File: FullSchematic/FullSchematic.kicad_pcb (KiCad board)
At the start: 2 copper layers, 106 parts, among them J1 USB_A, J10 LCD_Conn, J2 ATX-24, J3 Red Banana Jack, J4 Black Banana Jack, J5 2x6 Pin Header, J6 2x6 Pin Header, J7 CT3151-2, J8 CT3151-2, J9 2x6 Pin Header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

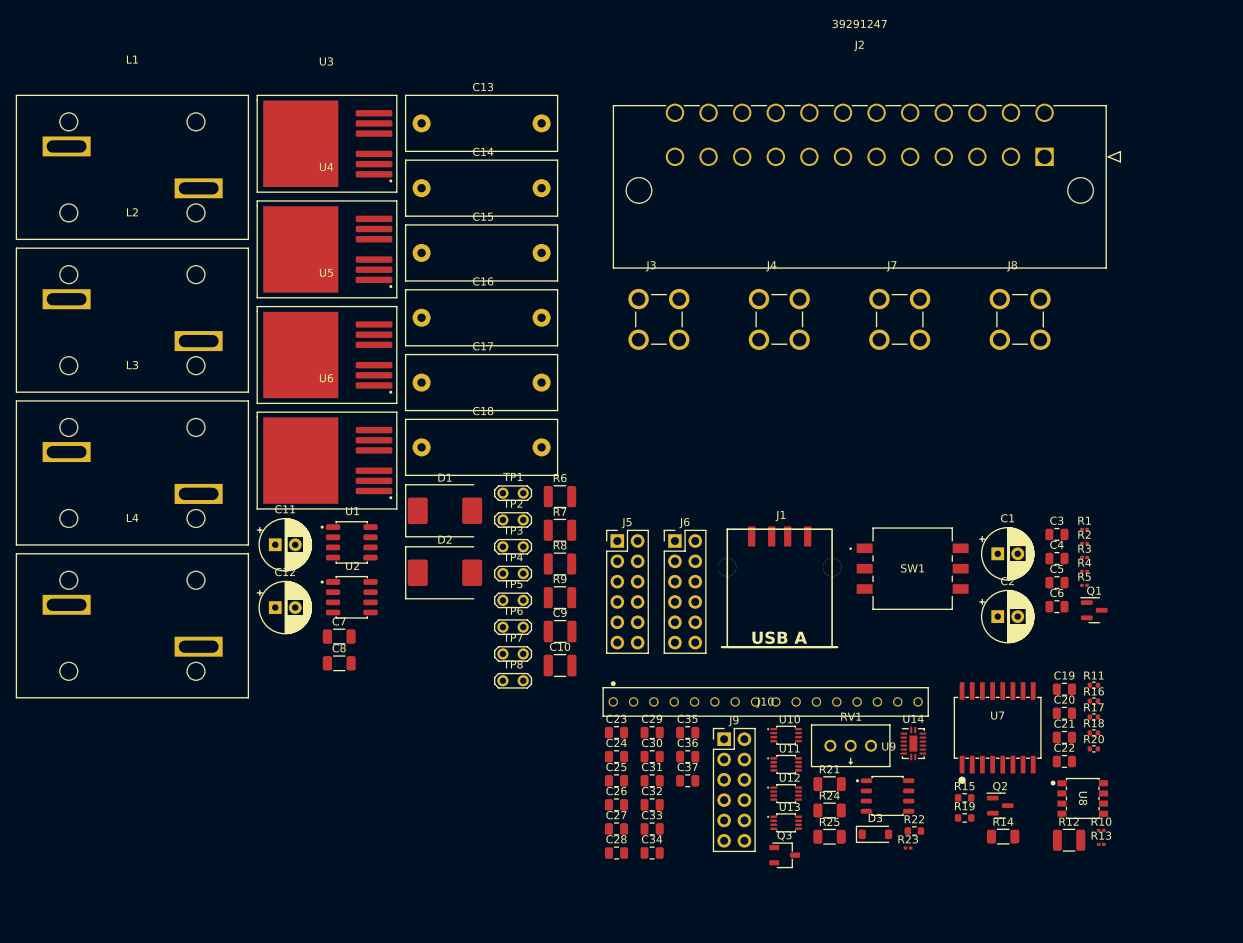
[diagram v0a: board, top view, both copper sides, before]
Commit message: Made PCB a 4-layer board
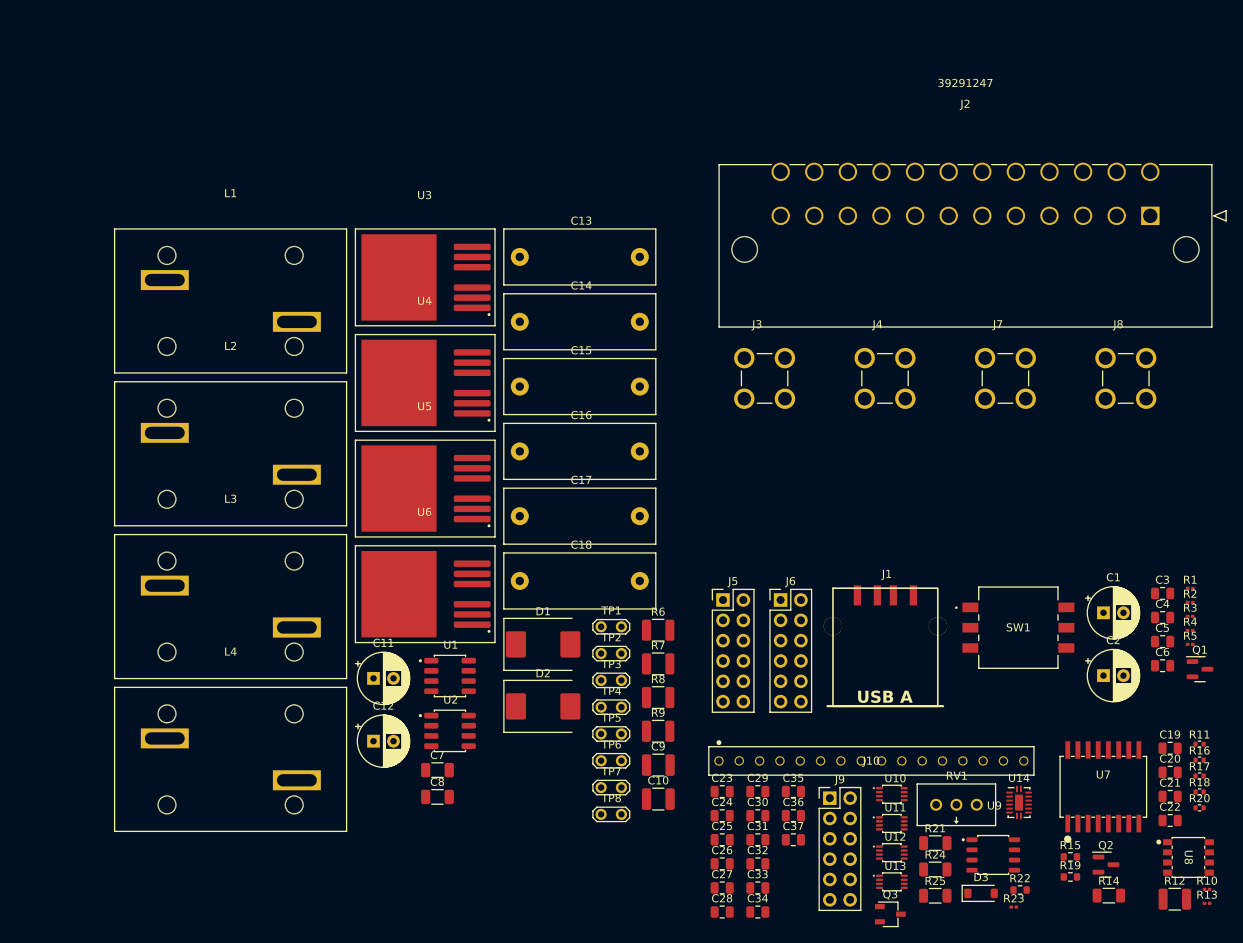
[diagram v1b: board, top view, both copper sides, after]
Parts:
- moved C13 20.7 mm to (145.1, 68.6)
- moved C14 20.7 mm to (145.1, 76.7)
- moved C16 20.7 mm to (145.1, 92.9)
- moved C17 20.7 mm to (145.1, 101.0)
- moved C18 20.7 mm to (145.1, 109.1)
- moved L1 20.7 mm to (101.4, 74.1)
- moved L2 20.7 mm to (101.4, 93.2)
- moved L4 20.7 mm to (101.4, 131.4)
- moved U3 20.7 mm to (122.5, 71.2)
- moved U4 20.7 mm to (122.5, 84.4)
- moved U6 20.7 mm to (122.5, 110.8)
- moved TP6 20.7 mm to (147.7, 131.6)
- moved C11 20.7 mm to (119.3, 121.3)
- moved C12 20.7 mm to (119.3, 129.2)
- moved C15 20.7 mm to (145.1, 84.8)
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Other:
- copper layers 2 -> 4

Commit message: Some Re-arrangements for Power Amplifier
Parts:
- moved C13 223.3 mm to (-74.0, 25.5)
- moved C14 223.3 mm to (-74.0, 33.6)
- moved C15 223.3 mm to (-74.0, 41.7)
- moved C16 223.3 mm to (-74.0, 49.8)
- moved C17 223.3 mm to (-74.0, 57.9)
- moved C18 223.3 mm to (-74.0, 66.0)
- moved C11 177.8 mm to (-58.0, 108.0)
- moved C12 177.8 mm to (-58.0, 115.9)
- moved C7 177.8 mm to (-50.0, 119.5)
- moved C8 177.8 mm to (-50.0, 122.8)
- moved TP1 177.8 mm to (-29.6, 101.6)
- moved TP2 177.8 mm to (-29.6, 104.9)
- moved TP3 177.8 mm to (-29.6, 108.3)
- moved TP4 177.8 mm to (-29.6, 111.6)
- moved TP5 177.8 mm to (-29.6, 115.0)
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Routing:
- net Net-(U1-HO): track 0.00 -> 12.0 mm

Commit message: First attempt at FET/Driver layout
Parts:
- moved C18 353.9 mm to (248.9, -78.8), turned to 90 degrees
- moved C16 337.8 mm to (238.4, -78.8), turned to 90 degrees
- moved C15 331.2 mm to (247.0, -39.5), turned to 90 degrees
- moved C17 330.5 mm to (226.9, -78.8), turned to 90 degrees
- moved C14 319.5 mm to (237.0, -39.5), turned to 90 degrees
- moved C13 305.4 mm to (219.1, -60.3), turned to 90 degrees
- moved TP1 274.0 mm to (152.5, -103.2)
- moved TP2 272.2 mm to (152.4, -97.5)
- moved TP3 269.3 mm to (152.3, -90.3)
- moved C11 268.9 mm to (124.2, -89.8)
- moved J1 265.7 mm to (7.29, -74.2)
- moved TP5 259.8 mm to (152.5, -70.4)
- moved TP7 259.8 mm to (152.5, -63.7)
- moved TP8 259.8 mm to (152.5, -60.4)
- moved C12 259.8 mm to (124.0, -69.5)
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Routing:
- net Net-(U2-VS): track 0.00 -> 122.0 mm, vias 0 -> 2
- net Net-(U1-VS): track 0.00 -> 118.0 mm, vias 0 -> 2
- net COM: track 0.00 -> 81.2 mm, vias 0 -> 6
- net Net-(U5-Gate): track 0.00 -> 37.0 mm
- net Net-(U3-Gate): track 0.00 -> 36.5 mm
- net Net-(U4-Gate): track 0.00 -> 34.2 mm
- net Net-(D1-K): track 0.00 -> 20.7 mm
- net Net-(U1-LO): track 0.00 -> 20.1 mm, vias 0 -> 2
- net +12V: track 0.00 -> 14.1 mm, vias 0 -> 2
- net Net-(U1-HO): track 12.0 -> 4.61 mm
- net Net-(D2-K): track 0.00 -> 4.62 mm
- net Net-(U2-HO): track 0.00 -> 4.36 mm
- added copper zone on In2.Cu, net +12V
- added copper zone on In1.Cu, net COM

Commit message: More Edits
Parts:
- moved J2 259.3 mm to (122.6, 46.2), turned to 180 degrees
- moved R9 85.6 mm to (183.8, 159.8)
- moved U6 85.6 mm to (199.4, 156.2)
- moved U2 85.6 mm to (175.5, 154.4)
- moved U5 85.6 mm to (199.4, 141.1)
- moved C10 85.6 mm to (175.2, 143.2)
- moved C8 85.6 mm to (175.4, 160.7)
- moved D2 85.6 mm to (165.7, 143.2)
- moved R8 85.6 mm to (183.7, 153.7)
- moved U4 33.6 mm to (161.4, 90.7), turned to -90 degrees
- moved U3 30.9 mm to (161.4, 66.8), turned to -90 degrees
- moved D1 30.1 mm to (124.9, 72.1)
- moved U1 30.1 mm to (134.2, 82.5)
- moved C7 30.1 mm to (134.4, 88.4)
- moved C9 30.1 mm to (134.4, 72.1)
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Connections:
- R6 pad 2: Net-(U3-Gate) -> Net-(U1-VS)
- U3 pad 1: Net-(U3-Gate) -> Net-(U1-VS)
- U3 pad TAB: +12V -> Net-(U1-VS)
- U4 pad 5: COM -> Net-(U1-VS)
- U4 pad 6: COM -> Net-(U1-VS)
- U4 pad 7: COM -> Net-(U1-VS)
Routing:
- net COM: track 81.2 -> 143.0 mm
- net Net-(U1-VS): track 118.0 -> 59.7 mm, vias 2 -> 3
- net Net-(U3-Gate): track 36.5 -> 0.00 mm
- net Net-(U4-Gate): track 34.2 -> 0.05 mm
- net Net-(U1-LO): track 20.1 -> 0.00 mm, vias 2 -> 0
- net Net-(D1-K): track 20.7 -> 4.62 mm
- net +12V: track 14.1 -> 3.50 mm, vias 2 -> 1
- net Net-(U1-HO): track 4.61 -> 0.00 mm

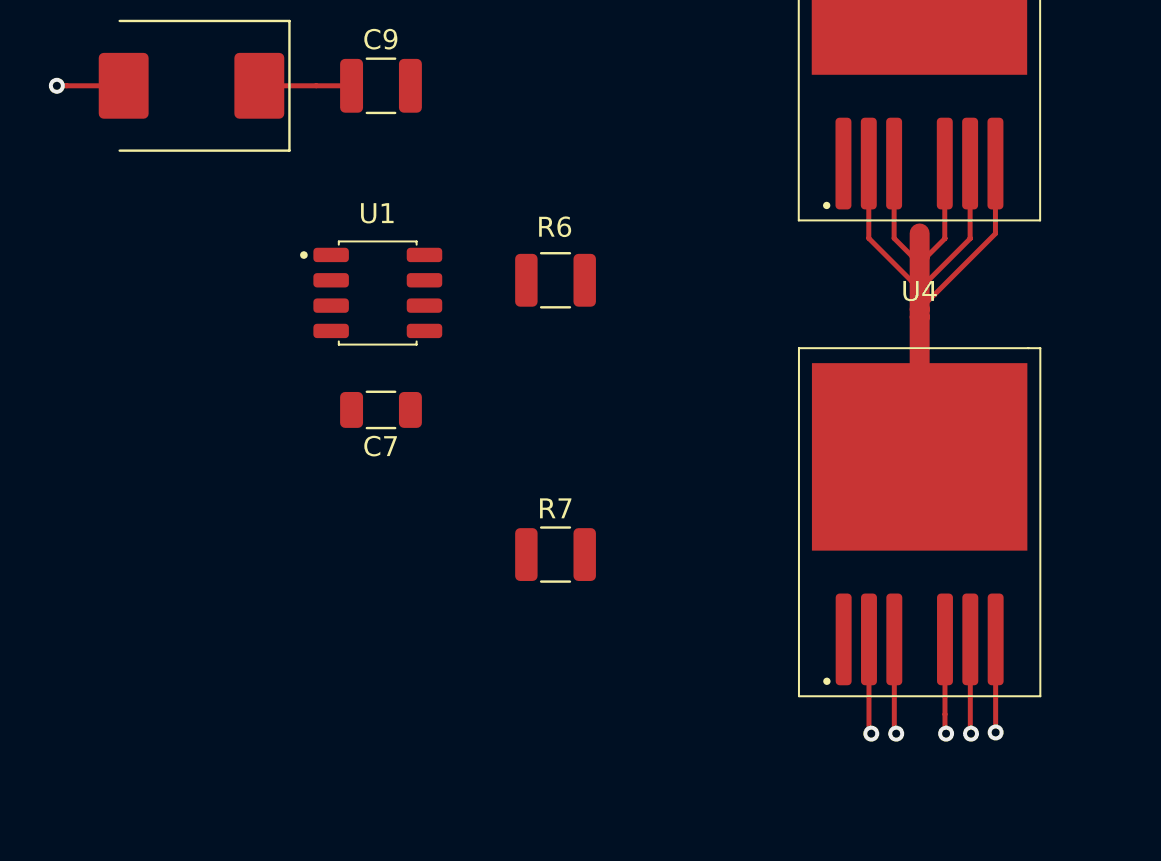
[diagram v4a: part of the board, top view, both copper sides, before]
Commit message: Added high-current power planes on all 4 layers for FETs
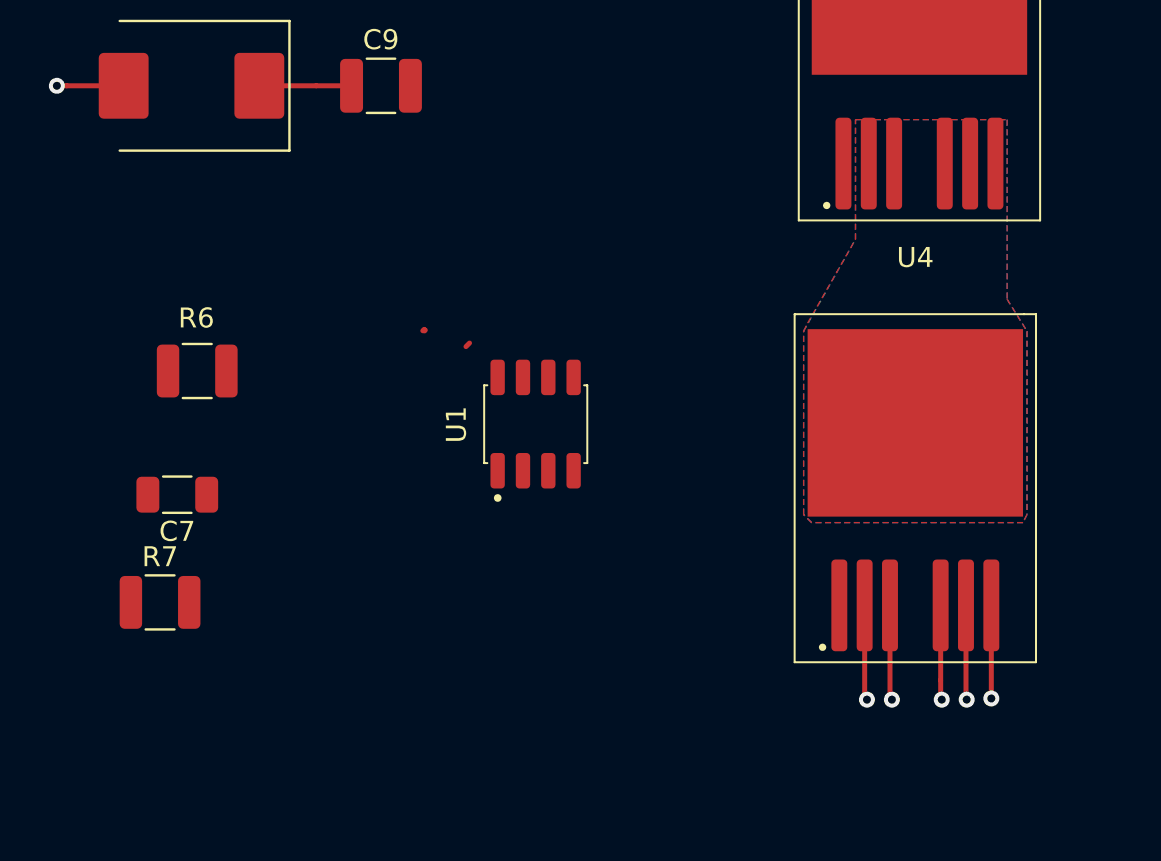
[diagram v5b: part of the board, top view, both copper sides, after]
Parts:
- moved R7 20.0 mm to (123.3, 98.0)
- moved R6 18.5 mm to (125.2, 86.4)
- moved C7 11.1 mm to (124.2, 92.6)
- moved U1 10.3 mm to (142.2, 89.1), turned to 90 degrees
- moved U4 1.72 mm to (161.2, 89.0)
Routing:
- net Net-(U1-VS): track 59.7 -> 32.7 mm
- added copper zone on B.Cu, net Net-(U1-VS)
- added copper zone on F.Cu, net Net-(U1-VS)
- added copper zone on In1.Cu, net Net-(U1-VS)
- added copper zone on In2.Cu, net Net-(U1-VS)
- removed copper zone on In2.Cu, net +12V
- removed copper zone on In1.Cu, net COM

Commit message: Corrected trace size for high current
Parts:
- moved J2 192.5 mm to (313.7, 68.9)
- moved U2 188.3 mm to (319.4, 32.9)
- moved U5 188.3 mm to (343.3, 19.6)
- moved U6 188.3 mm to (343.3, 34.7)
- moved C10 188.3 mm to (319.1, 21.7)
- moved C8 188.3 mm to (319.3, 39.2)
- moved D2 188.3 mm to (309.6, 21.7)
- moved R8 188.3 mm to (327.6, 32.2)
- moved R9 188.3 mm to (327.6, 38.3)
- moved L4 92.4 mm to (186.9, 72.0)
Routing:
- net COM: track 143.0 -> 109.2 mm, vias 6 -> 2
- net Net-(D1-K): track 4.62 -> 0.00 mm
